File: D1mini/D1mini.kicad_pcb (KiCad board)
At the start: 2 copper layers, 108.5 x 66.5 mm, 18 parts, among them J1 USB_B, U1 LM555xN, U2 LM555xN

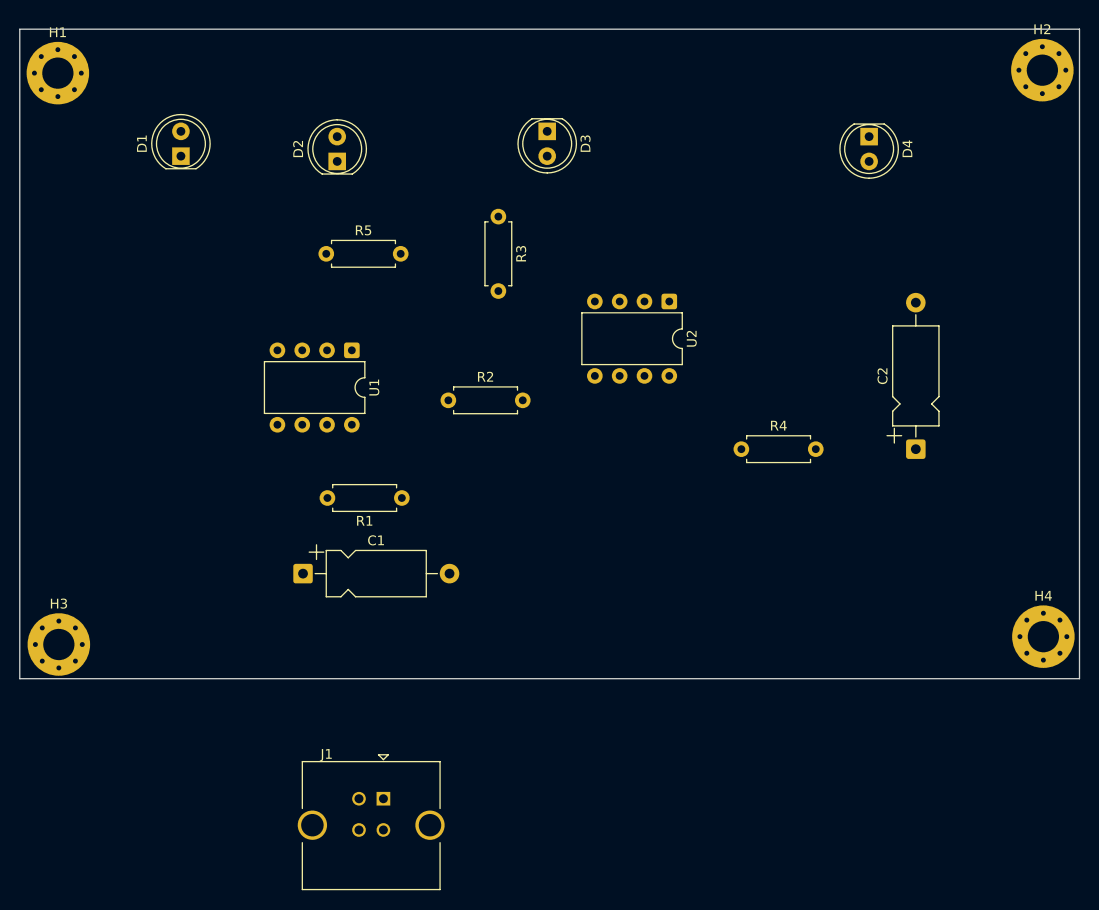
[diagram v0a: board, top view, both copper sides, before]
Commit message: 新增新專案, usb to TTL
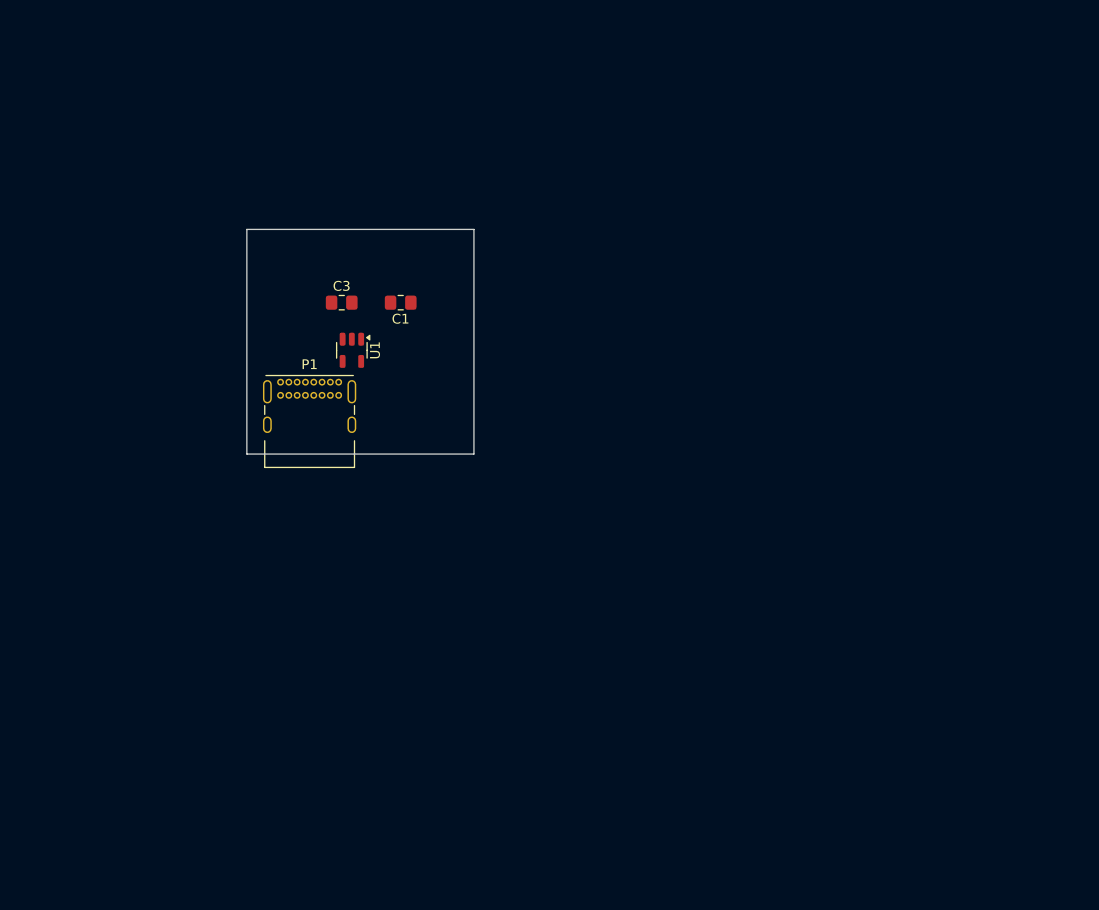
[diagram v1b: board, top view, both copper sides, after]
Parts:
- removed C2: 100u, Capacitor_THT:CP_Axial_L10.0mm_D4.5mm_P15.00mm_Horizontal
- removed D1, D2, D3, D4: LED_Filled, LED_THT:LED_D5.0mm_Clear
- removed H1, H2, H3, H4: MountingHole, MountingHole:MountingHole_3.2mm_M3_Pad_Via
- removed J1: USB_B, Connector_USB:USB_B_TE_5787834_Vertical
- removed R1, R3: 1k, Resistor_THT:R_Axial_DIN0207_L6.3mm_D2.5mm_P7.62mm_Horizontal
- removed R2, R4: 10k, Resistor_THT:R_Axial_DIN0207_L6.3mm_D2.5mm_P7.62mm_Horizontal
- removed R5: 10, Resistor_THT:R_Axial_DIN0207_L6.3mm_D2.5mm_P7.62mm_Horizontal
- removed U2: LM555xN, Package_DIP:DIP-8_W7.62mm
- added C3: 1u, Capacitor_SMD:C_0805_2012Metric_Pad1.18x1.45mm_HandSolder, F.Cu at (179.0, 45.0)
- added P1: USB_C_Plug_USB2.0, Connector_USB:USB_C_Receptacle_GCT_USB4085, F.Cu at (172.7, 53.1)
- C1: value 100u -> 1u; footprint Capacitor_THT:CP_Axial_L10.0mm_D4.5mm_P15.00mm_Horizontal -> Capacitor_SMD:C_0805_2012Metric_Pad1.18x1.45mm_HandSolder
- U1: value LM555xN -> ME6211C33M5; footprint Package_DIP:DIP-8_W7.62mm -> Package_TO_SOT_SMD:SOT-23-5
- moved C1 29.5 mm to (185.0, 45.0), turned to 180 degrees
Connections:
- C1 pad 1: Net-(U1-THR) -> /+3V3
- C1 pad 2: GND -> GNDREF
- U1 pad 1: GND -> +5Vfe
- U1 pad 2: Net-(U1-THR) -> GNDREF
- U1 pad 3: Net-(U1-Q) -> +5Vfe
- U1 pad 4: VCC -> unconnected-(U1-NC-Pad4)
- U1 pad 5: unconnected-(U1-CV-Pad5) -> /+3V3
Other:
- board size 108.5 x 66.5 mm -> 23.2 x 23 mm
